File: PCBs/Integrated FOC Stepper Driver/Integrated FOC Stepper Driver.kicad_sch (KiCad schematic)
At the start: 64 parts, among them J1 INPUT, J2 USB C Receptacle, J3 OUTPUT, J4 MOTOR, J5 Conn_01x02, SW1 RESET, SW2 BOOT, U1 SE8650X2-HF, U2 SE8650X2-HF, U3 W25Q128JVS, U4 RP2040, U5 SN65HVD1050D, U6 MT6701CT, Y1 12MHz/12pF/50Ω/20ppm

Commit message: V1 of driver PCB
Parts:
- removed C10: 100n, Capacitor_SMD:C_0603_1608Metric_Pad1.08x0.95mm_HandSolder, symbol Device:C
- removed D1: LED, LED_SMD:LED_0603_1608Metric_Pad1.05x0.95mm_HandSolder, symbol Device:LED
- removed D3, D4: D_Schottky, Diode_SMD:D_SMA_Handsoldering, symbol Device:D_Schottky
- removed D5: TVS (6V), symbol Device:D_TVS
- removed R1: 10k, Resistor_SMD:R_0603_1608Metric_Pad0.98x0.95mm_HandSolder, symbol Device:R
- removed R5: 1K, Resistor_SMD:R_0603_1608Metric_Pad0.98x0.95mm_HandSolder, symbol Device:R
- removed R6: 10K, Resistor_SMD:R_0603_1608Metric_Pad0.98x0.95mm_HandSolder, symbol Device:R
- removed U1: SE8650X2-HF, Package_TO_SOT_SMD:SOT-23_Handsoldering, symbol Regulator_Linear:AMS1117
- removed U3: W25Q128JVS, Package_SO:SOIC-8_5.23x5.23mm_P1.27mm, symbol Memory_Flash:W25Q128JVS
- added C17, C21, C6: 100nF, Capacitor_SMD:C_0402_1005Metric_Pad0.74x0.62mm_HandSolder, symbol Device:C
- added D2: WS2812B, LED_SMD:LED_WS2812B_PLCC4_5.0x5.0mm_P3.2mm, symbol LED:WS2812B
- added D3: BAT54C, Package_TO_SOT_SMD:SOT-23_Handsoldering, symbol Device:D_Dual_CommonCathode_AAK_Parallel
- added R7: 1k, Resistor_SMD:R_0402_1005Metric_Pad0.72x0.64mm_HandSolder, symbol Device:R
- added R8: 10k, Resistor_SMD:R_0402_1005Metric_Pad0.72x0.64mm_HandSolder, symbol Device:R
- added U1: PJ54M50SE, Package_TO_SOT_SMD:SOT-23-5_HandSoldering, symbol EchoSymbols:PJ54M50SE
- added U4: W25Q128JVS, Package_SO:SOIC-8_5.23x5.23mm_P1.27mm, symbol Memory_Flash:W25Q128JVS
- C1, C2, C5: LCSC (none) -> C15849
- C10: renamed from C11; value 100n -> 100nF; footprint Capacitor_SMD:C_0603_1608Metric_Pad1.08x0.95mm_HandSolder -> Capacitor_SMD:C_0402_1005Metric_Pad0.74x0.62mm_HandSolder; LCSC (none) -> C307331
- C11: renamed from C8; value 100n -> 100nF; footprint Capacitor_SMD:C_0603_1608Metric_Pad1.08x0.95mm_HandSolder -> Capacitor_SMD:C_0402_1005Metric_Pad0.74x0.62mm_HandSolder; LCSC (none) -> C307331
- C12: renamed from C7; value 100n -> 100nF; footprint Capacitor_SMD:C_0603_1608Metric_Pad1.08x0.95mm_HandSolder -> Capacitor_SMD:C_0402_1005Metric_Pad0.74x0.62mm_HandSolder; LCSC (none) -> C307331
- C13: renamed from C6; value 100n -> 100nF; footprint Capacitor_SMD:C_0603_1608Metric_Pad1.08x0.95mm_HandSolder -> Capacitor_SMD:C_0402_1005Metric_Pad0.74x0.62mm_HandSolder; LCSC (none) -> C307331
- C14: renamed from C16; value 100n -> 100nF; footprint Capacitor_SMD:C_0603_1608Metric_Pad1.08x0.95mm_HandSolder -> Capacitor_SMD:C_0402_1005Metric_Pad0.74x0.62mm_HandSolder; LCSC (none) -> C307331
- C15: renamed from C18; value 100n -> 100nF; footprint Capacitor_SMD:C_0603_1608Metric_Pad1.08x0.95mm_HandSolder -> Capacitor_SMD:C_0402_1005Metric_Pad0.74x0.62mm_HandSolder; LCSC (none) -> C307331
- C16: renamed from C9; footprint Capacitor_SMD:C_0603_1608Metric_Pad1.08x0.95mm_HandSolder -> Capacitor_SMD:C_0402_1005Metric_Pad0.74x0.62mm_HandSolder; LCSC (none) -> C29266
- C18: renamed from C13; value 22p -> 22pF; footprint Capacitor_SMD:C_0603_1608Metric_Pad1.08x0.95mm_HandSolder -> Capacitor_SMD:C_0402_1005Metric_Pad0.74x0.62mm_HandSolder
- C19: renamed from C14; value 22p -> 22pF; footprint Capacitor_SMD:C_0603_1608Metric_Pad1.08x0.95mm_HandSolder -> Capacitor_SMD:C_0402_1005Metric_Pad0.74x0.62mm_HandSolder
- C20: renamed from C15; footprint Capacitor_SMD:C_0603_1608Metric_Pad1.08x0.95mm_HandSolder -> Capacitor_SMD:C_0402_1005Metric_Pad0.74x0.62mm_HandSolder; LCSC (none) -> C29266
- C22: renamed from C20; footprint Capacitor_SMD:C_0603_1608Metric_Pad1.08x0.95mm_HandSolder -> Capacitor_SMD:C_2220_5750Metric_Pad1.97x5.40mm_HandSolder; LCSC (none) -> C2932476
- C23: renamed from C21; footprint Capacitor_SMD:C_0603_1608Metric_Pad1.08x0.95mm_HandSolder -> Capacitor_SMD:C_2220_5750Metric_Pad1.97x5.40mm_HandSolder; LCSC (none) -> C2932476
- C24: renamed from C23; footprint Capacitor_SMD:C_0603_1608Metric_Pad1.08x0.95mm_HandSolder -> Capacitor_SMD:C_0402_1005Metric_Pad0.74x0.62mm_HandSolder; LCSC (none) -> C307331
- C25: renamed from C24; footprint Capacitor_SMD:C_0603_1608Metric_Pad1.08x0.95mm_HandSolder -> Capacitor_SMD:C_0402_1005Metric_Pad0.74x0.62mm_HandSolder; LCSC (none) -> C307331
- C26: renamed from C22; footprint Capacitor_SMD:C_0603_1608Metric_Pad1.08x0.95mm_HandSolder -> Capacitor_SMD:C_0402_1005Metric_Pad0.74x0.62mm_HandSolder; LCSC (none) -> C307331
- C3: value 100n -> 100nF; footprint Capacitor_SMD:C_0603_1608Metric_Pad1.08x0.95mm_HandSolder -> Capacitor_SMD:C_0402_1005Metric_Pad0.74x0.62mm_HandSolder; LCSC (none) -> C307331
- C4: value 1uF -> 10uF; LCSC (none) -> C96446
- C7: renamed from C19; value 100n -> 100nF; footprint Capacitor_SMD:C_0603_1608Metric_Pad1.08x0.95mm_HandSolder -> Capacitor_SMD:C_0402_1005Metric_Pad0.74x0.62mm_HandSolder; LCSC (none) -> C307331
- C8: renamed from C17; value 100n -> 100nF; footprint Capacitor_SMD:C_0603_1608Metric_Pad1.08x0.95mm_HandSolder -> Capacitor_SMD:C_0402_1005Metric_Pad0.74x0.62mm_HandSolder; LCSC (none) -> C307331
- C9: renamed from C12; value 100n -> 100nF; footprint Capacitor_SMD:C_0603_1608Metric_Pad1.08x0.95mm_HandSolder -> Capacitor_SMD:C_0402_1005Metric_Pad0.74x0.62mm_HandSolder; LCSC (none) -> C307331
- J1, J3: footprint Connector_JST:JST_PH_S4B-PH-SM4-TB_1x04-1MP_P2.00mm_Horizontal -> Connector_JST:JST_PH_S4B-PH-K_1x04_P2.00mm_Horizontal; LCSC (none) -> C157926
- J2: symbol Connector:USB_C_Receptacle_USB2.0 -> Connector:USB_C_Receptacle_USB2.0_16P
- J4: LCSC (none) -> C2763695
- J5: LCSC (none) -> C706874
- R1: renamed from R2; value 500 -> 523; footprint Resistor_SMD:R_0805_2012Metric_Pad1.20x1.40mm_HandSolder -> Resistor_SMD:R_0402_1005Metric_Pad0.72x0.64mm_HandSolder; LCSC (none) -> C517803
- R10: renamed from R11; footprint Resistor_SMD:R_0603_1608Metric_Pad0.98x0.95mm_HandSolder -> Resistor_SMD:R_0402_1005Metric_Pad0.72x0.64mm_HandSolder; LCSC (none) -> C114758
- R11: renamed from R12; footprint Resistor_SMD:R_0603_1608Metric_Pad0.98x0.95mm_HandSolder -> Resistor_SMD:R_0402_1005Metric_Pad0.72x0.64mm_HandSolder; LCSC (none) -> C477765
- R12: renamed from R13; footprint Resistor_SMD:R_0603_1608Metric_Pad0.98x0.95mm_HandSolder -> Resistor_SMD:R_0402_1005Metric_Pad0.72x0.64mm_HandSolder; LCSC (none) -> C477765
- R13: renamed from R14; value 500 -> 523; footprint Resistor_SMD:R_0805_2012Metric_Pad1.20x1.40mm_HandSolder -> Resistor_SMD:R_0402_1005Metric_Pad0.72x0.64mm_HandSolder; LCSC (none) -> C517803
- R14: renamed from R15; value 500 -> 523; footprint Resistor_SMD:R_0805_2012Metric_Pad1.20x1.40mm_HandSolder -> Resistor_SMD:R_0402_1005Metric_Pad0.72x0.64mm_HandSolder; LCSC (none) -> C517803
- R2: renamed from R3; footprint Resistor_SMD:R_0603_1608Metric_Pad0.98x0.95mm_HandSolder -> Resistor_SMD:R_0402_1005Metric_Pad0.72x0.64mm_HandSolder
- R3: renamed from R4; footprint Resistor_SMD:R_0603_1608Metric_Pad0.98x0.95mm_HandSolder -> Resistor_SMD:R_0402_1005Metric_Pad0.72x0.64mm_HandSolder
- R4: renamed from R7; footprint Resistor_SMD:R_0603_1608Metric_Pad0.98x0.95mm_HandSolder -> Resistor_SMD:R_0402_1005Metric_Pad0.72x0.64mm_HandSolder; LCSC C153109 -> C60490
- R5: renamed from R8; footprint Resistor_SMD:R_0603_1608Metric_Pad0.98x0.95mm_HandSolder -> Resistor_SMD:R_0402_1005Metric_Pad0.72x0.64mm_HandSolder; LCSC (none) -> C274349
- R6: renamed from R9; footprint Resistor_SMD:R_0603_1608Metric_Pad0.98x0.95mm_HandSolder -> Resistor_SMD:R_0402_1005Metric_Pad0.72x0.64mm_HandSolder; LCSC (none) -> C274349
- R9: renamed from R10; footprint Resistor_SMD:R_0603_1608Metric_Pad0.98x0.95mm_HandSolder -> Resistor_SMD:R_0402_1005Metric_Pad0.72x0.64mm_HandSolder; LCSC C98841 -> C106235
- U2: value SE8650X2-HF -> PJ9500M33SA; LCSC (none) -> C20618178
- U3: renamed from U4; LCSC (none) -> C2040
- Y1: LCSC C2450215 -> C258938
- renumbered D2 to D1, SW2 to SW1, SW1 to SW2
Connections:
- net +3.3V: now also C17.1, C6.1, D2.1 (VDD), R8.2, U4.8 (VCC)
- net +5V: now also C21.1, D3.3 (K)
- net A1: now also J4.2 (Pin_2); no longer J4.1 (Pin_1)
- net A2: now also J4.1 (Pin_1); no longer J4.2 (Pin_2)
- net B1: now also J4.4 (Pin_4); no longer J4.3 (Pin_3)
- net B2: now also J4.3 (Pin_3); no longer J4.4 (Pin_4)
- net GND: now also U7.9 (GND), U8.9 (GND), C17.2, C21.2, C6.2, D2.3 (VSS), U1.2 (GND), U4.4 (GND); no longer U7.PAD (GND), U8.PAD (GND)
- net NEOPIXEL: now also R1.2; no longer R1.1
- net QSPI_SCK: now also U4.6 (CLK)
- net QSPI_SD0: now also U4.5 (DI(IO0))
- net QSPI_SD1: now also U4.2 (DO(IO1))
- net QSPI_SD2: now also U4.3 (IO2)
- net QSPI_SD3: now also U4.7 (IO3)
- net QSPI_SS: now also R7.2, R8.1, U4.1 (~{CS})
- net VBUS: now also U1.1 (VIN), U1.3 (EN)
- net ~{USB_BOOT}: now also R7.1
- net VUSB: now reaches J2.A4 (VBUS), J2.A9 (VBUS), J2.B4 (VBUS), J2.B9 (VBUS)
- net VUSB: now also D3.1 (A)
- net at D1.4 (DIN): now also R1.1; no longer R1.2
- net at C4.1: now also D3.2 (A), U1.5 (VOUT)
- net at D1.2 (DOUT): now also D2.4 (DIN)
- net USB_DN: now reaches R6.1, U3.46 (USB_DM)
- net USB_DP: now reaches R5.2, U3.47 (USB_DP)
- net LED: no longer names the net of U3.16 (GPIO13)
- no-connect marks 21 -> 22
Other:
- moved on the sheet: C10, C11, C12, C13, C14, C15, C23, C24, C25, C26, C7, C8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

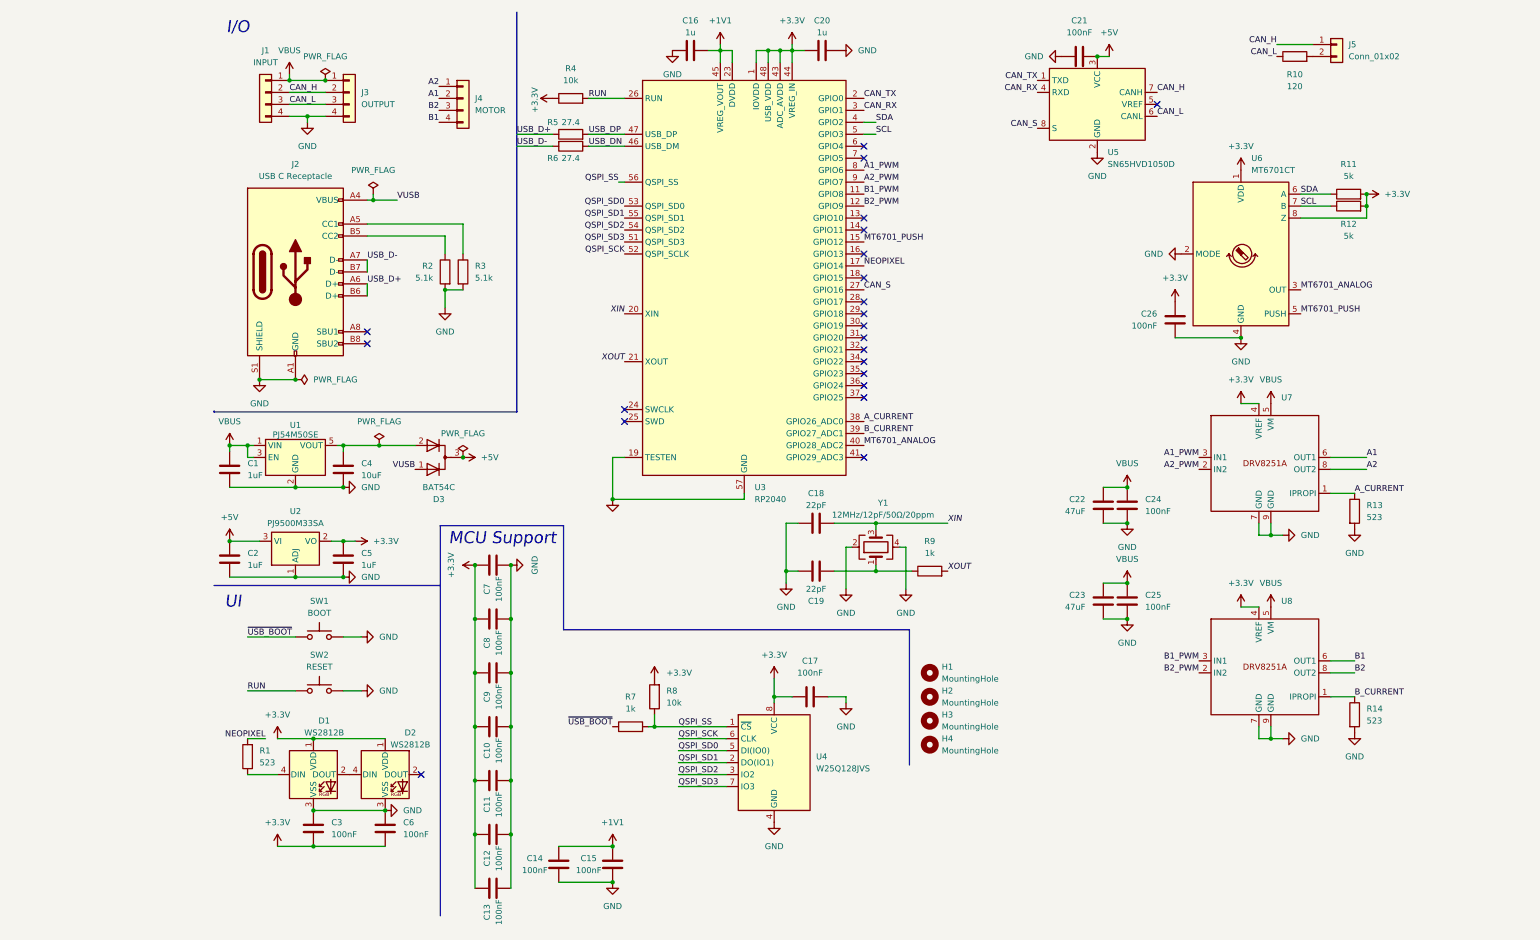
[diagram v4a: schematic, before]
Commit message: Clean up schematic, remove all 0.4/0.2mm vias from layout
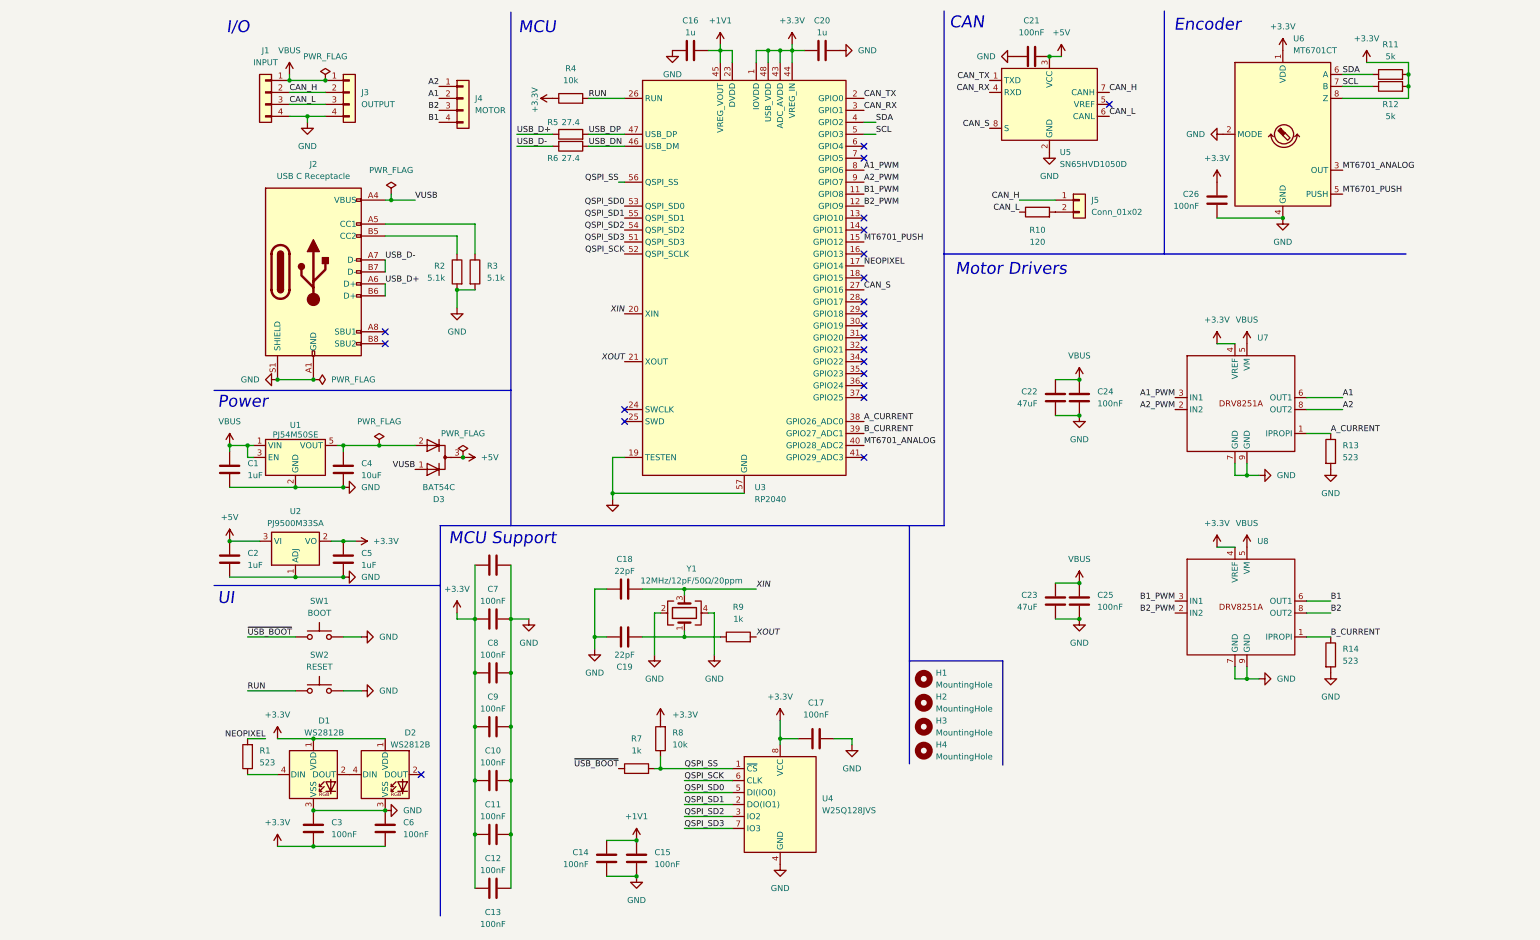
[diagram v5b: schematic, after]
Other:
- note added: "CAN"
- note added: "Encoder"
- note added: "MCU"
- note added: "Motor Drivers"
- note added: "Power"
- moved on the sheet: C14, C15, C17, C21, C22, C23, C24, C25, C26, J2, J5, R10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

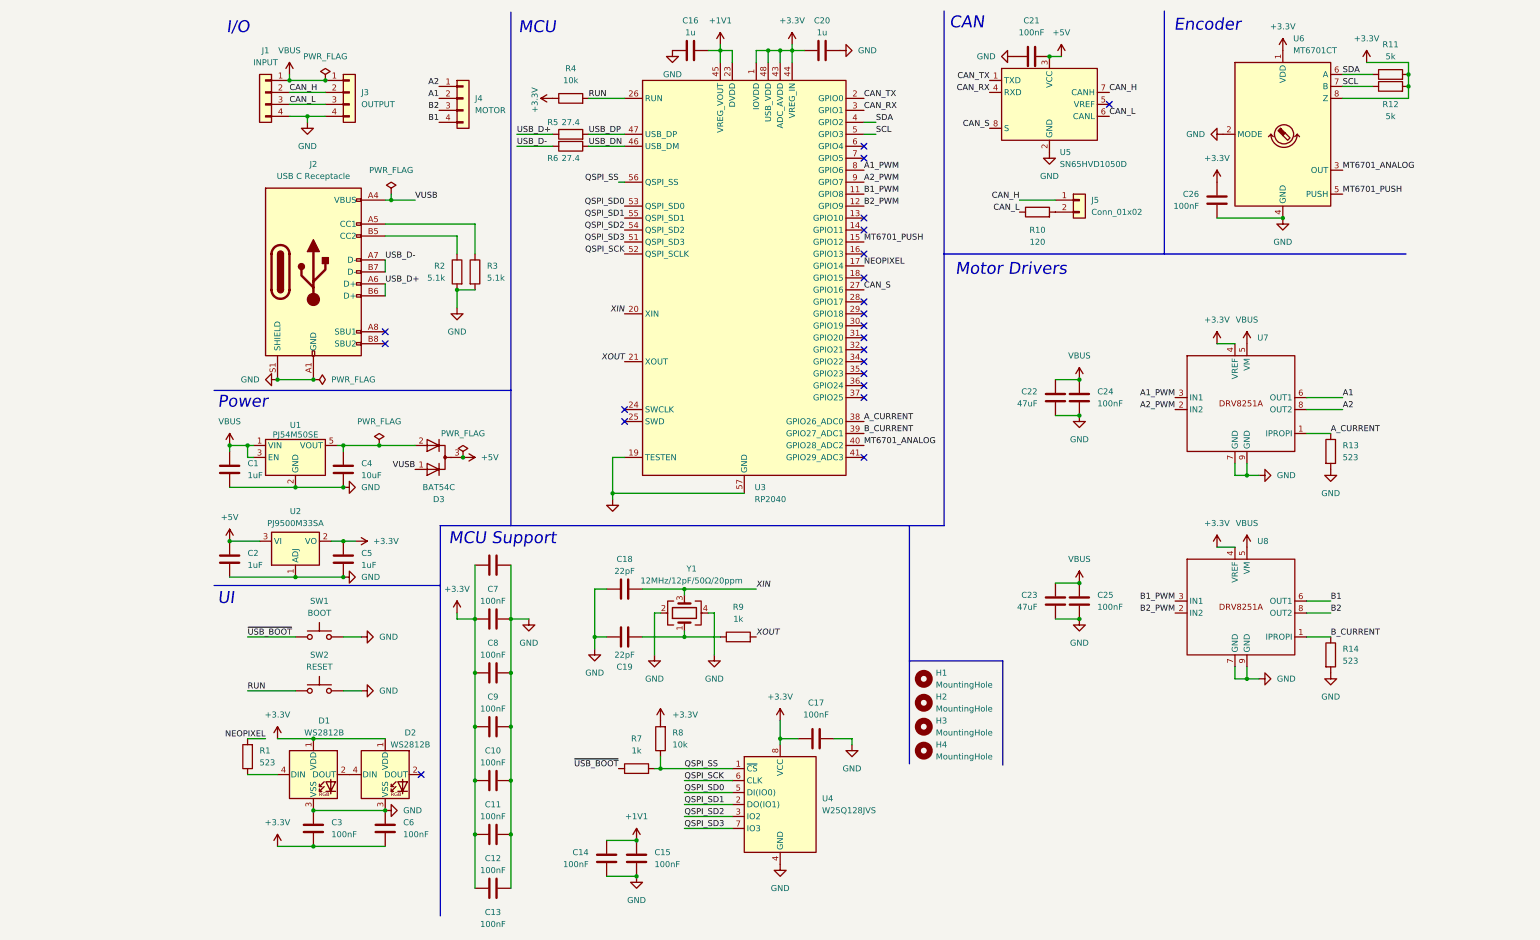
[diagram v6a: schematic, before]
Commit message: Layout V2
Added a voltage divider from VBUS to measure up to 48V on ADC
Switch motor connector to JST-XH at 3A instead of 2A
Relayout to accomodate changes
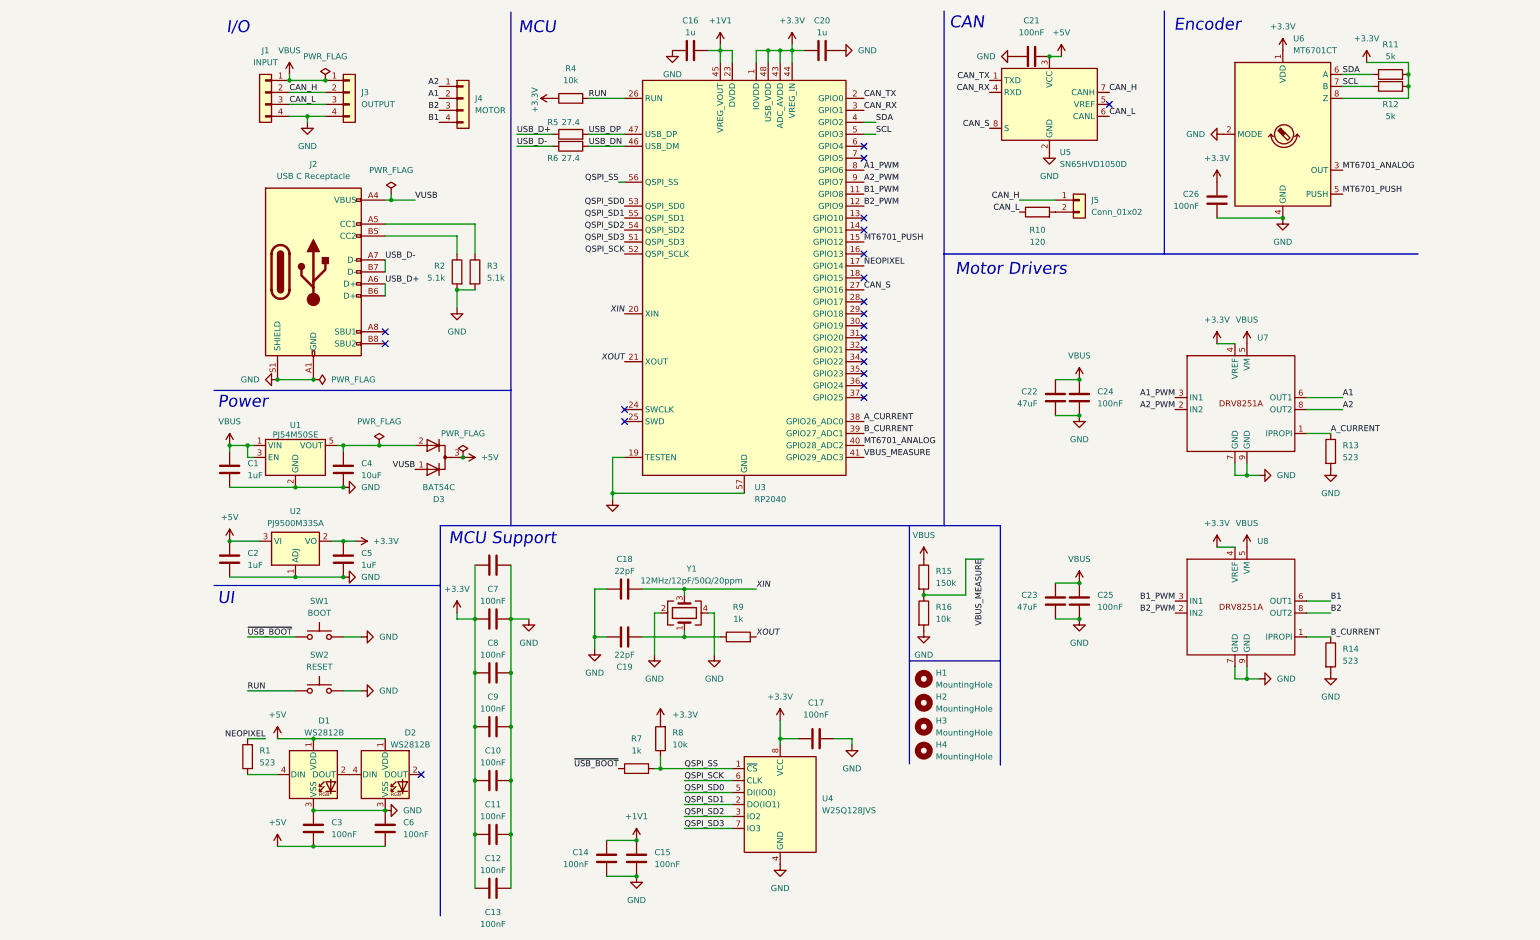
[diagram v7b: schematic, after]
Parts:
- added R15: 150k, Resistor_SMD:R_0402_1005Metric, symbol Device:R
- added R16: 10k, Resistor_SMD:R_0402_1005Metric, symbol Device:R
- C1, C2, C4, C5: footprint Capacitor_SMD:C_0603_1608Metric_Pad1.08x0.95mm_HandSolder -> Capacitor_SMD:C_0603_1608Metric
- C10, C11, C12, C13, C14, C15, C16, C17, C18, C19, C20, C21, C24, C25, C26, C3, C6, C7, C8, C9: footprint Capacitor_SMD:C_0402_1005Metric_Pad0.74x0.62mm_HandSolder -> Capacitor_SMD:C_0402_1005Metric
- C22, C23: footprint Capacitor_SMD:C_2220_5750Metric_Pad1.97x5.40mm_HandSolder -> Capacitor_SMD:C_2220_5750Metric
- D3, U2: footprint Package_TO_SOT_SMD:SOT-23_Handsoldering -> Package_TO_SOT_SMD:SOT-23
- J4: footprint Connector_JST:JST_PH_S4B-PH-SM4-TB_1x04-1MP_P2.00mm_Horizontal -> Connector_JST:JST_XH_S4B-XH-SM4-TB_1x04-1MP_P2.50mm_Horizontal; LCSC C2763695 -> C2831798
- R1, R10, R11, R12, R13, R14, R2, R3, R4, R5, R6, R7, R8, R9: footprint Resistor_SMD:R_0402_1005Metric_Pad0.72x0.64mm_HandSolder -> Resistor_SMD:R_0402_1005Metric
- U1: footprint Package_TO_SOT_SMD:SOT-23-5_HandSoldering -> Package_TO_SOT_SMD:SOT-23-5
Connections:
- net +3.3V: no longer C3.1, C6.1, D1.1 (VDD), D2.1 (VDD)
- net +5V: now also C3.1, C6.1, D1.1 (VDD), D2.1 (VDD)
- net GND: now also R16.2
- net VBUS: now also R15.1
- net VBUS_MEASURE: now reaches U3.41 (GPIO29_ADC3)
- net VBUS_MEASURE: now also R15.2, R16.1
- no-connect marks 22 -> 21
